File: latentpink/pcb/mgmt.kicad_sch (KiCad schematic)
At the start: 82 parts, among them J10 XILINX_JTAG, J11 FAN_01, J12 FAN_01, J15 CONN_01X03, J16 JUMPER_0402_SPDT, J17 JUMPER_0402_SPDT, J23 PMOD_HOST, J7 RJ45, U2 XC7K160T-2FBG484C, U20 AT24MAC402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

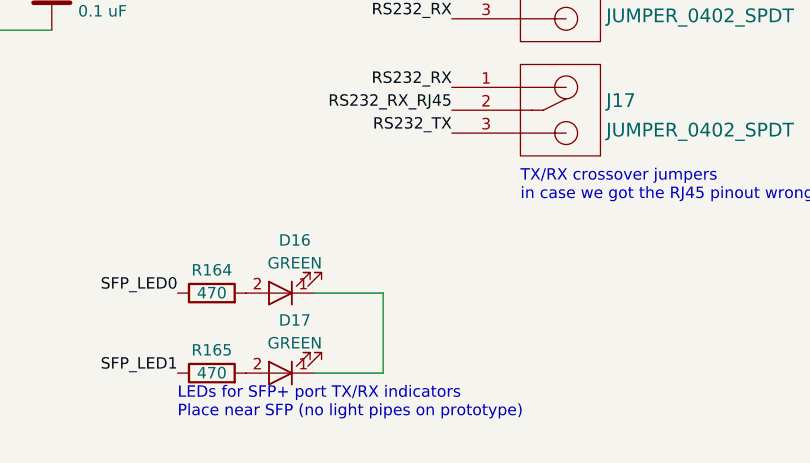
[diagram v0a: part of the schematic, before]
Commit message: Progress on management / power region at south
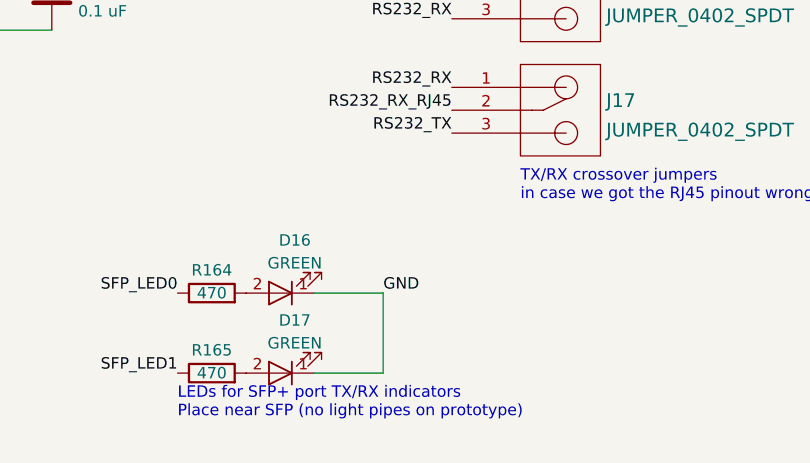
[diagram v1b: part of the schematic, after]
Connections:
- net GND: now also D16.1 (K), D17.1 (K)
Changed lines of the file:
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@@
     (effects (font (size 1.27 1.27)) (justify right bottom))
+  )
+  (label "GND" (at 200.66 264.16 0)
+    (effects (font (size 1.27 1.27)) (justify left bottom))
   )
   (label "3V3" (at 35.56 90.17 180)

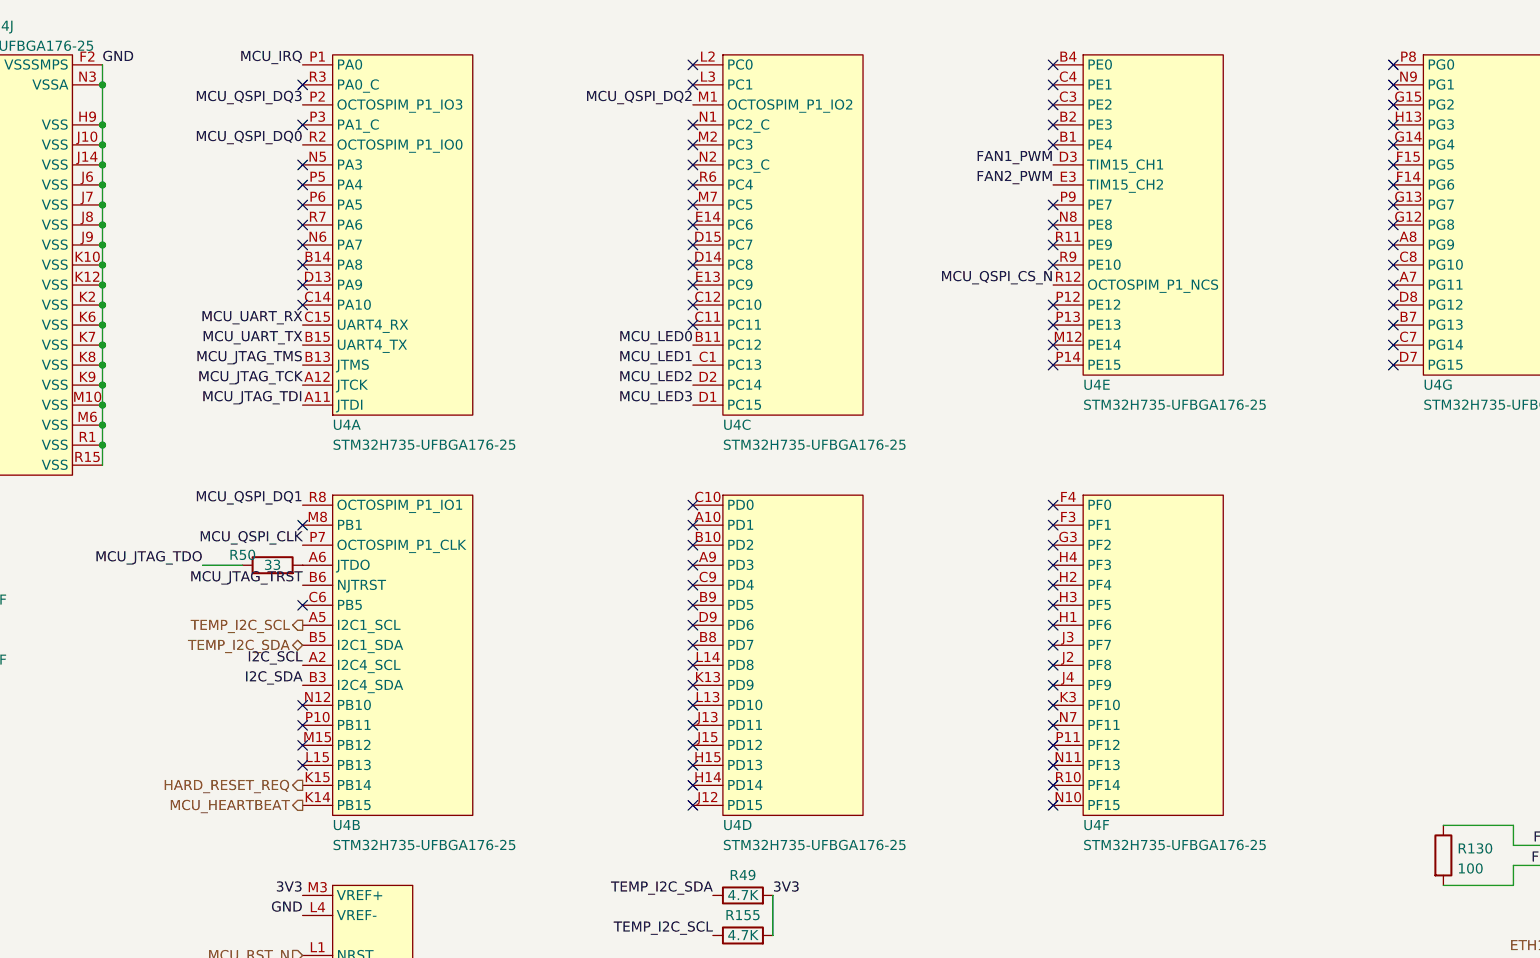
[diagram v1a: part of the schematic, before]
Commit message: Continued work on management MCU area
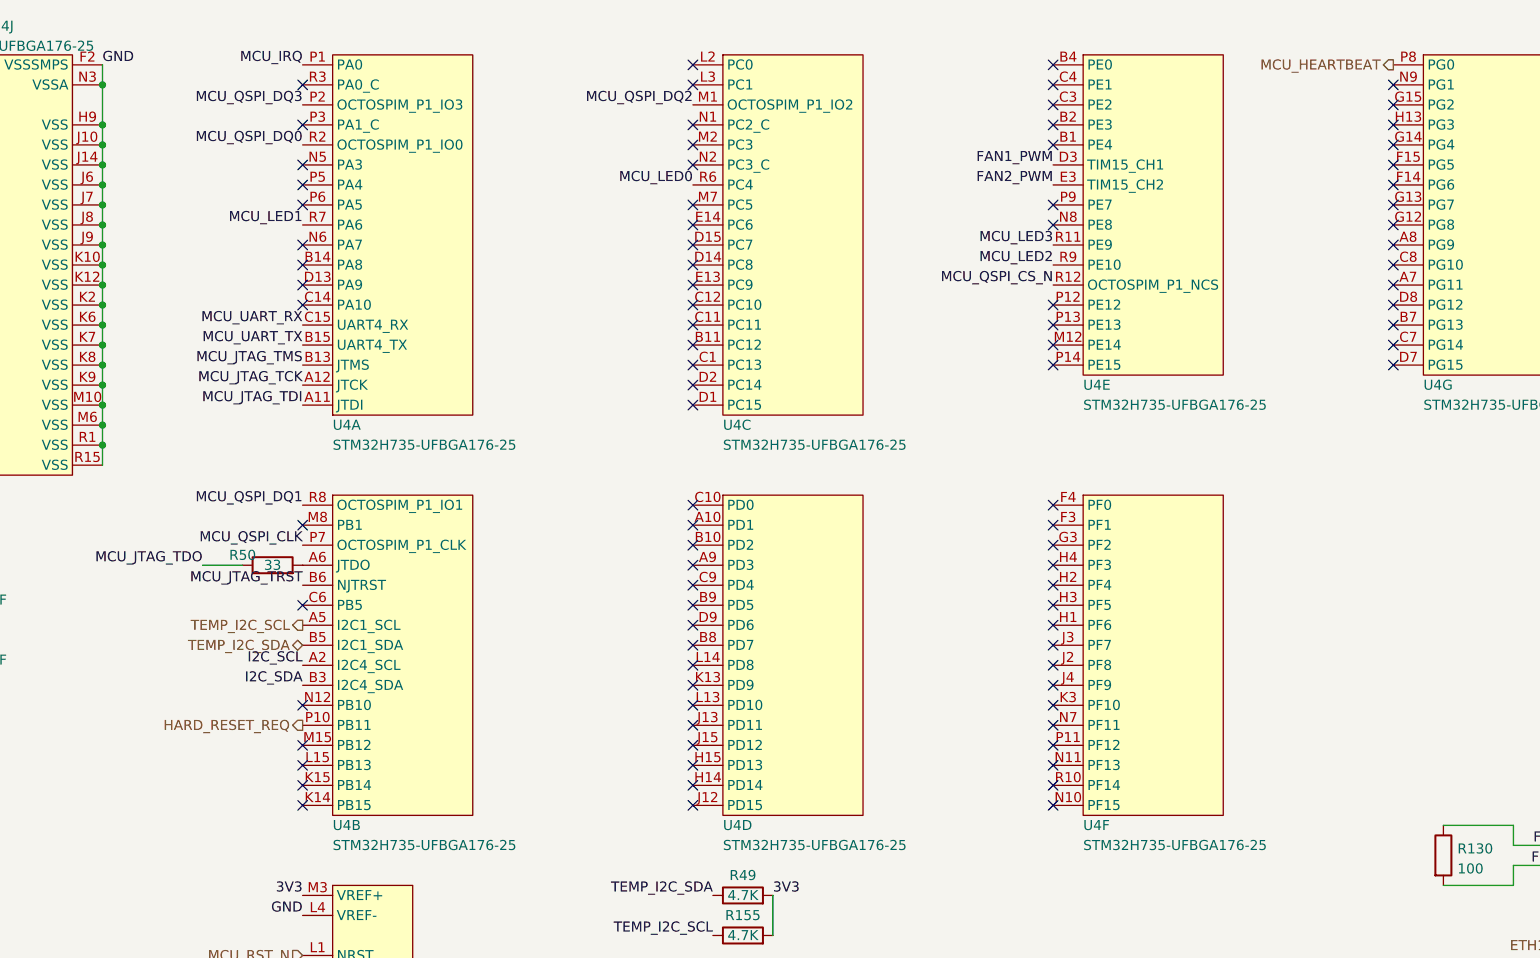
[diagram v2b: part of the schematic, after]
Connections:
- net HARD_RESET_REQ: now also U4.P10 (PB11); no longer U4.K15 (PB14)
- net MCU_HEARTBEAT: now also U4.P8 (PG0); no longer U4.K14 (PB15)
- net MCU_LED0: now also U4.R6 (PC4); no longer U4.B11 (PC12)
- net MCU_LED1: now also U4.R7 (PA6); no longer U4.C1 (PC13)
- net MCU_LED2: now also U4.R9 (PE10); no longer U4.D2 (PC14)
- net MCU_LED3: now also U4.R11 (PE9); no longer U4.D1 (PC15)
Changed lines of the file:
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@@
   (no_connect (at 214.63 119.38))
   (no_connect (at 303.53 66.04))
-  (no_connect (at 165.1 48.26))
   (no_connect (at 214.63 106.68))
   (no_connect (at 214.63 48.26))
@@
   (no_connect (at 165.1 109.22))
   (no_connect (at 214.63 109.22))
-  (no_connect (at 214.63 43.18))
   (no_connect (at 260.35 83.82))
   (no_connect (at 165.1 58.42))
@@
   (no_connect (at 214.63 91.44))
   (no_connect (at 214.63 30.48))
+  (no_connect (at 214.63 63.5))
   (no_connect (at 214.63 111.76))
   (no_connect (at 260.35 121.92))
@@
   (no_connect (at 214.63 58.42))
   (no_connect (at 335.28 154.94))
+  (no_connect (at 165.1 121.92))
   (no_connect (at 260.35 27.94))
   (no_connect (at 260.35 58.42))
+  (no_connect (at 214.63 68.58))
   (no_connect (at 260.35 109.22))
   (no_connect (at 303.53 38.1))
@@
   (no_connect (at 303.53 60.96))
   (no_connect (at 165.1 114.3))
+  (no_connect (at 165.1 119.38))
   (no_connect (at 260.35 86.36))
   (no_connect (at 165.1 55.88))
@@
   (no_connect (at 260.35 116.84))
   (no_connect (at 260.35 114.3))
-  (no_connect (at 260.35 50.8))
   (no_connect (at 214.63 101.6))
   (no_connect (at 335.28 124.46))
@@
   (no_connect (at 165.1 50.8))
   (no_connect (at 260.35 99.06))
-  (no_connect (at 303.53 27.94))
   (no_connect (at 303.53 53.34))
   (no_connect (at 212.09 217.17))
+  (no_connect (at 214.63 66.04))
   (no_connect (at 214.63 35.56))
   (no_connect (at 260.35 119.38))
@@
   (no_connect (at 214.63 53.34))
   (no_connect (at 214.63 114.3))
+  (no_connect (at 214.63 71.12))
   (no_connect (at 260.35 66.04))
-  (no_connect (at 260.35 53.34))
   (no_connect (at 260.35 30.48))
   (no_connect (at 260.35 48.26))
@@
   (no_connect (at 260.35 106.68))
   (no_connect (at 212.09 199.39))
-  (no_connect (at 165.1 111.76))
   (no_connect (at 165.1 116.84))
   (no_connect (at 260.35 96.52))
@@
     (effects (font (size 1.27 1.27)) (justify right bottom))
   )
-  (label "MCU_LED1" (at 214.63 66.04 180)
+  (label "MCU_LED1" (at 165.1 48.26 180)
     (effects (font (size 1.27 1.27)) (justify right bottom))
   )
@@
     (effects (font (size 1.27 1.27)) (justify right bottom))
   )
-  (label "MCU_LED3" (at 214.63 71.12 180)
+  (label "MCU_LED3" (at 260.35 50.8 180)
     (effects (font (size 1.27 1.27)) (justify right bottom))
   )
@@
     (effects (font (size 1.27 1.27)) (justify left bottom))
   )
-  (label "MCU_LED0" (at 214.63 63.5 180)
+  (label "MCU_LED0" (at 214.63 43.18 180)
     (effects (font (size 1.27 1.27)) (justify right bottom))
   )
@@
     (effects (font (size 1.27 1.27)) (justify right bottom))
   )
-  (label "MCU_LED2" (at 214.63 68.58 180)
+  (label "MCU_LED2" (at 260.35 53.34 180)
     (effects (font (size 1.27 1.27)) (justify right bottom))
   )
@@
     (effects (font (size 1.27 1.27)) (justify right))
   )
-  (hierarchical_label "HARD_RESET_REQ" (shape output) (at 165.1 119.38 180)
+  (hierarchical_label "HARD_RESET_REQ" (shape output) (at 165.1 111.76 180)
     (effects (font (size 1.27 1.27)) (justify right))
   )
@@
     (effects (font (size 1.27 1.27)) (justify right))
   )
-  (hierarchical_label "MCU_HEARTBEAT" (shape output) (at 165.1 121.92 180)
+  (hierarchical_label "MCU_HEARTBEAT" (shape output) (at 303.53 27.94 180)
     (effects (font (size 1.27 1.27)) (justify right))
   )

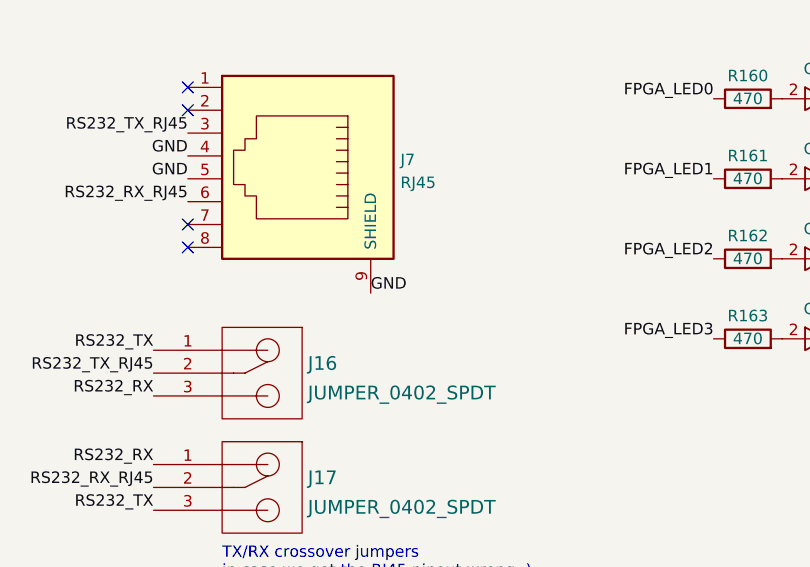
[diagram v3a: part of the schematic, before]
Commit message: Hooked up some more PHY stuff plus management UART transceiver
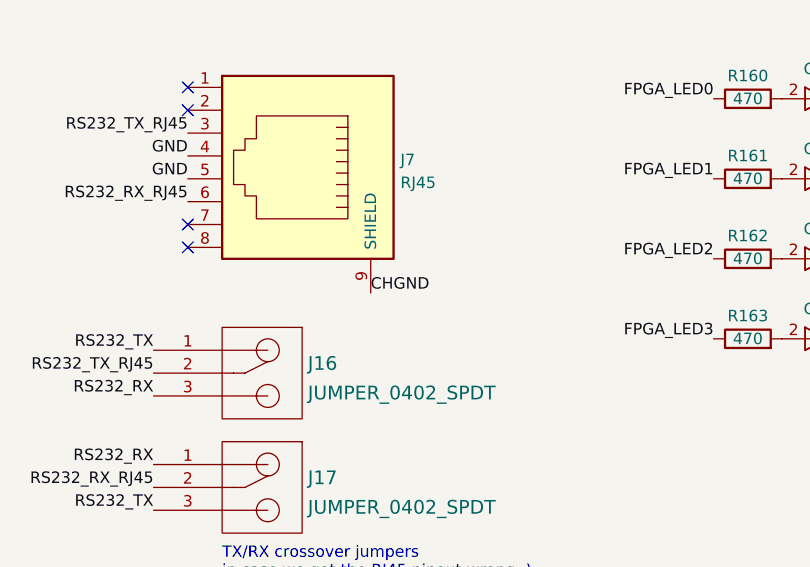
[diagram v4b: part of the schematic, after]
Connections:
- net CHGND: now also J7.9 (SHIELD)
- net GND: no longer J7.9 (SHIELD)
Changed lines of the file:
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@@
     (effects (font (size 1.27 1.27)) (justify right bottom))
   )
-  (label "GND" (at 232.41 222.25 0)
+  (label "CHGND" (at 232.41 222.25 0)
     (effects (font (size 1.27 1.27)) (justify left bottom))
   )

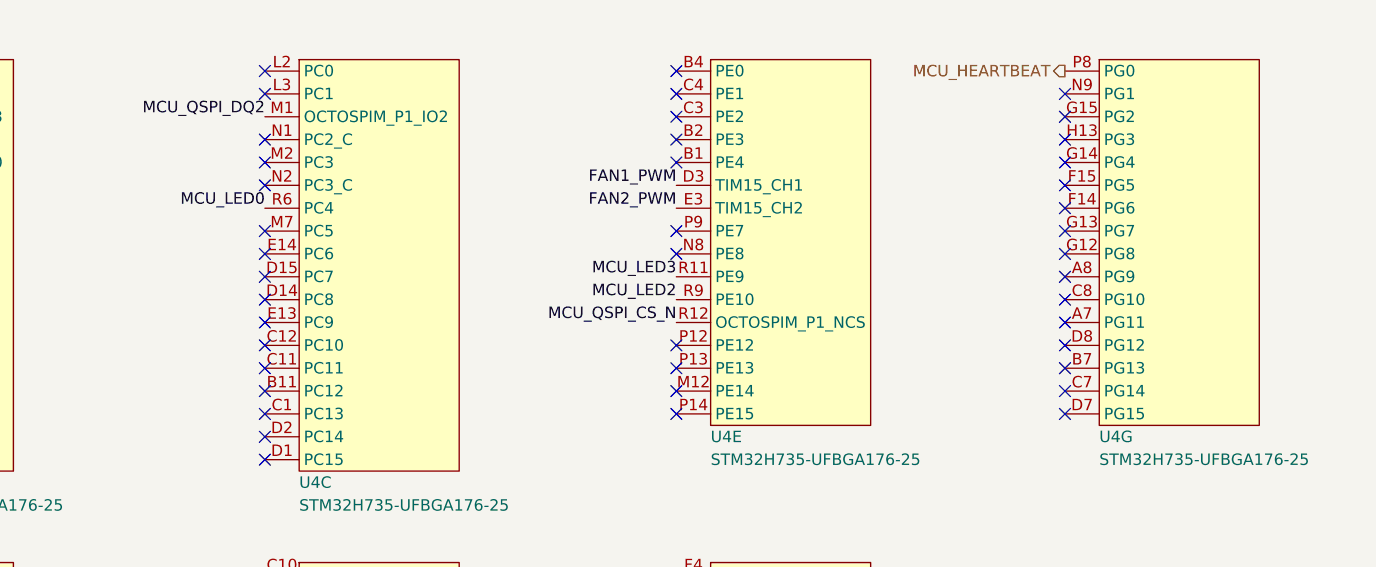
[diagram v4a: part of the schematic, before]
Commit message: VSC8512 LED layout
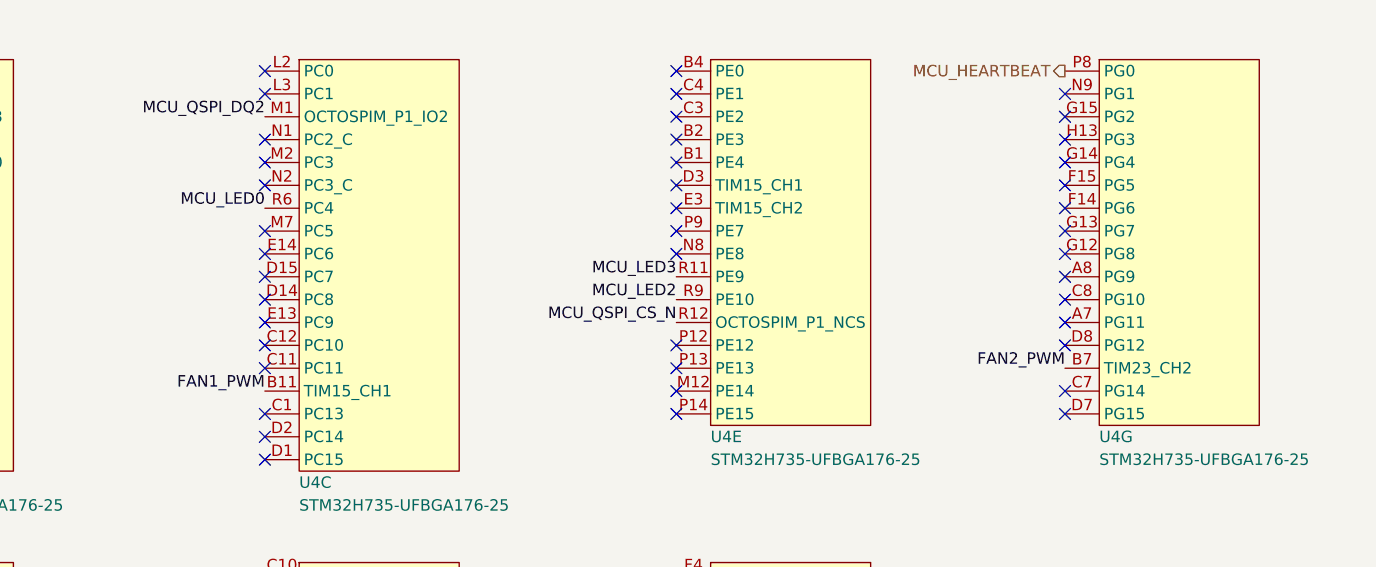
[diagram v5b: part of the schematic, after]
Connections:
- net FAN1_PWM: now also U4.B11 (PC12); no longer U4.D3 (PE5)
- net FAN2_PWM: now also U4.B7 (PG13); no longer U4.E3 (PE6)
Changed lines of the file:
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@@
   (no_connect (at 303.53 50.8))
   (no_connect (at 214.63 91.44))
+  (no_connect (at 260.35 40.64))
   (no_connect (at 214.63 30.48))
-  (no_connect (at 214.63 63.5))
+  (no_connect (at 260.35 43.18))
   (no_connect (at 214.63 111.76))
   (no_connect (at 260.35 121.92))
@@
   (no_connect (at 303.53 33.02))
   (no_connect (at 165.1 53.34))
-  (no_connect (at 303.53 60.96))
   (no_connect (at 165.1 114.3))
   (no_connect (at 165.1 119.38))
@@
     (effects (font (size 1.27 1.27)) (justify right bottom))
   )
-  (label "FAN2_PWM" (at 260.35 43.18 180)
+  (label "FAN2_PWM" (at 303.53 60.96 180)
     (effects (font (size 1.27 1.27)) (justify right bottom))
   )
@@
     (effects (font (size 1.27 1.27)) (justify right bottom))
   )
-  (label "FAN1_PWM" (at 260.35 40.64 180)
+  (label "FAN1_PWM" (at 214.63 63.5 180)
     (effects (font (size 1.27 1.27)) (justify right bottom))
   )
@@
     (pin "P7" (alternate "OCTOSPIM_P1_CLK"))
     (pin "R8" (alternate "OCTOSPIM_P1_IO1"))
-    (pin "B11")
+    (pin "B11" (alternate "TIM15_CH1"))
     (pin "C1")
     (pin "C11")
@@
     (pin "A7")
     (pin "A8")
-    (pin "B7")
+    (pin "B7" (alternate "TIM23_CH2"))
     (pin "C7")
     (pin "C8")
@@
     (pin "P7" (alternate "OCTOSPIM_P1_CLK"))
     (pin "R8" (alternate "OCTOSPIM_P1_IO1"))
-    (pin "B11")
+    (pin "B11" (alternate "TIM15_CH1"))
     (pin "C1")
     (pin "C11")
@@
     (pin "A7")
     (pin "A8")
-    (pin "B7")
+    (pin "B7" (alternate "TIM23_CH2"))
     (pin "C7")
     (pin "C8")
@@
     (pin "P7" (alternate "OCTOSPIM_P1_CLK"))
     (pin "R8" (alternate "OCTOSPIM_P1_IO1"))
-    (pin "B11")
+    (pin "B11" (alternate "TIM15_CH1"))
     (pin "C1")
     (pin "C11")
@@
     (pin "A7")
     (pin "A8")
-    (pin "B7")
+    (pin "B7" (alternate "TIM23_CH2"))
     (pin "C7")
     (pin "C8")
@@
     (pin "P7" (alternate "OCTOSPIM_P1_CLK"))
     (pin "R8" (alternate "OCTOSPIM_P1_IO1"))
-    (pin "B11")
+    (pin "B11" (alternate "TIM15_CH1"))
     (pin "C1")
     (pin "C11")
@@
     (pin "A7")
     (pin "A8")
-    (pin "B7")
+    (pin "B7" (alternate "TIM23_CH2"))
     (pin "C7")
     (pin "C8")
@@
     (pin "P7" (alternate "OCTOSPIM_P1_CLK"))
     (pin "R8" (alternate "OCTOSPIM_P1_IO1"))
-    (pin "B11")
+    (pin "B11" (alternate "TIM15_CH1"))
     (pin "C1")
     (pin "C11")
@@
     (pin "A7")
     (pin "A8")
-    (pin "B7")
+    (pin "B7" (alternate "TIM23_CH2"))
     (pin "C7")
     (pin "C8")
@@
     (pin "P7" (alternate "OCTOSPIM_P1_CLK"))
     (pin "R8" (alternate "OCTOSPIM_P1_IO1"))
-    (pin "B11")
+    (pin "B11" (alternate "TIM15_CH1"))
     (pin "C1")
     (pin "C11")
@@
     (pin "A7")
     (pin "A8")
-    (pin "B7")
+    (pin "B7" (alternate "TIM23_CH2"))
     (pin "C7")
     (pin "C8")
@@
     (pin "P7" (alternate "OCTOSPIM_P1_CLK"))
     (pin "R8" (alternate "OCTOSPIM_P1_IO1"))
-    (pin "B11")
+    (pin "B11" (alternate "TIM15_CH1"))
     (pin "C1")
     (pin "C11")
@@
     (pin "A7")
     (pin "A8")
-    (pin "B7")
+    (pin "B7" (alternate "TIM23_CH2"))
     (pin "C7")
     (pin "C8")
@@
     (pin "P7" (alternate "OCTOSPIM_P1_CLK"))
     (pin "R8" (alternate "OCTOSPIM_P1_IO1"))
-    (pin "B11")
+    (pin "B11" (alternate "TIM15_CH1"))
     (pin "C1")
     (pin "C11")
@@
     (pin "A7")
     (pin "A8")
-    (pin "B7")
+    (pin "B7" (alternate "TIM23_CH2"))
     (pin "C7")
     (pin "C8")
@@
     (pin "P7" (alternate "OCTOSPIM_P1_CLK"))
     (pin "R8" (alternate "OCTOSPIM_P1_IO1"))
-    (pin "B11")
+    (pin "B11" (alternate "TIM15_CH1"))
     (pin "C1")
     (pin "C11")
@@
     (pin "A7")
     (pin "A8")
-    (pin "B7")
+    (pin "B7" (alternate "TIM23_CH2"))
     (pin "C7")
     (pin "C8")
@@
     (pin "P7" (alternate "OCTOSPIM_P1_CLK"))
     (pin "R8" (alternate "OCTOSPIM_P1_IO1"))
-    (pin "B11")
+    (pin "B11" (alternate "TIM15_CH1"))
     (pin "C1")
     (pin "C11")
@@
     (pin "A7")
     (pin "A8")
-    (pin "B7")
+    (pin "B7" (alternate "TIM23_CH2"))
     (pin "C7")
     (pin "C8")

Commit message: Hooked up more low speed stuff, fan PWM, LEDs, power, etc. mostly in northeast corner
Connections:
- net MCU_QSPI_CLK: now also U2.E8 (IO_24_T3_16); no longer U2.A8 (IO_L21N_T3_DQS_16)
- net MCU_QSPI_CS_N: now also U2.B8 (IO_L22N_T3_16); no longer U2.E8 (IO_24_T3_16)
- net MCU_QSPI_DQ1: now also U2.A8 (IO_L21N_T3_DQS_16); no longer U2.B8 (IO_L22N_T3_16)
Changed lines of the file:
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@@
   (paper "A3")
   (title_block
-    (date "2023-05-28")
+    (date "2023-05-31")
     (rev "0.1")
     (company "Antikernel Labs")
@@
     (effects (font (size 1.27 1.27)) (justify right bottom))
   )
-  (label "MCU_QSPI_DQ1" (at 335.28 177.8 180)
+  (label "MCU_QSPI_DQ1" (at 335.28 172.72 180)
     (effects (font (size 1.27 1.27)) (justify right bottom))
   )
@@
     (effects (font (size 1.27 1.27)) (justify right bottom))
   )
-  (label "MCU_QSPI_CS_N" (at 335.28 185.42 180)
+  (label "MCU_QSPI_CS_N" (at 335.28 177.8 180)
     (effects (font (size 1.27 1.27)) (justify right bottom))
   )
@@
     (effects (font (size 1.27 1.27)) (justify right bottom))
   )
-  (label "MCU_QSPI_CLK" (at 335.28 172.72 180)
-    (effects (font (size 1.27 1.27)) (justify right bottom))
-  )
+  (label "MCU_QSPI_CLK" (at 335.28 185.42 180)
+    (effects (font (size 1.27 1.27)) (justify right bottom))
+  )
